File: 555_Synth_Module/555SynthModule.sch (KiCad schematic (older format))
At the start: 32 parts, among them J1 Conn_01x09_Male, Q1 2N3904, Q2 2N3904, Q3 2N3904, Q4 2N3904, Q5 2N3904, U1 NE555P, U2 LM741

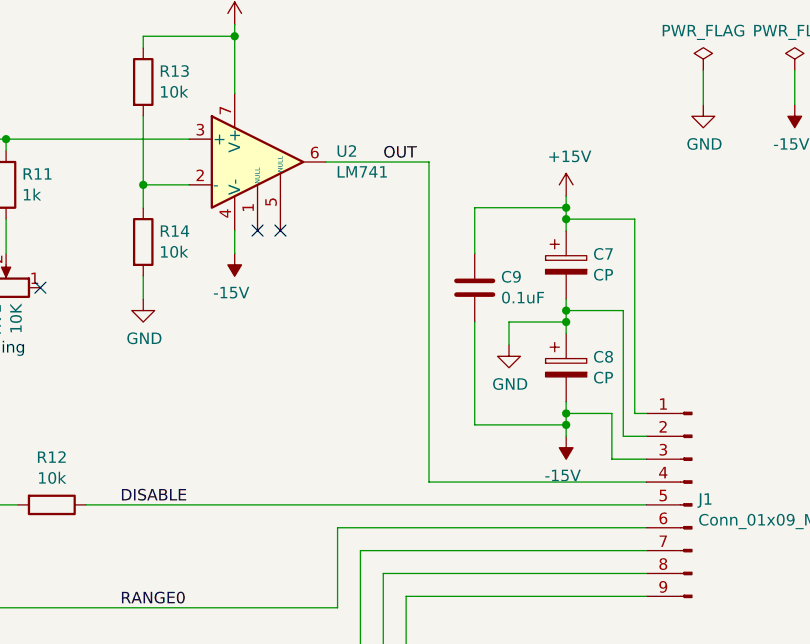
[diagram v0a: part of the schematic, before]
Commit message: Resolved Issue #3 Also: * Added output cap to 555 modules * EnvelopeFilter now has an output cap
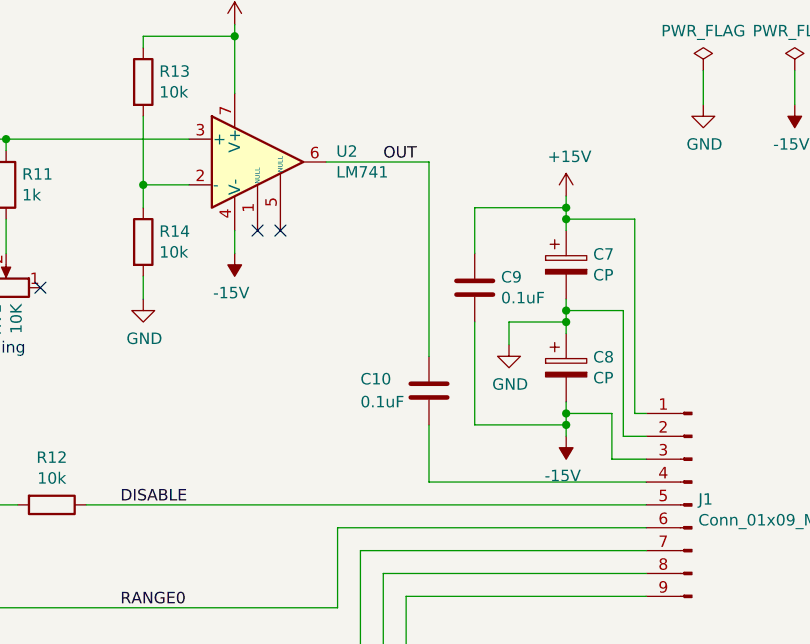
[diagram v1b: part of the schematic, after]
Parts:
- added C10: 0.1uF, Capacitor_THT:C_Disc_D4.3mm_W1.9mm_P5.00mm, symbol Device:C
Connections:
- net OUT: now also C10.1; no longer J1.4 (Pin_4)
- new net: C10.2, J1.4 (Pin_4)
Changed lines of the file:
@@
 	6950 2550 7400 2550
 Wire Wire Line
-	7400 2550 7400 3950
+	7400 2550 7400 3400
 $Comp
 L power:-15V #PWR0107
@@
 Wire Wire Line
 	5900 4050 8350 4050
+$Comp
+L Device:C C10
+U 1 1 602BE631
+P 7400 3550
+F 0 "C10" H 7100 3600 50  0000 L CNN
+F 1 "0.1uF" H 7100 3500 50  0000 L CNN
+F 2 "Capacitor_THT:C_Disc_D4.3mm_W1.9mm_P5.00mm" H 7438 3400 50  0001 C CNN
+F 3 "~" H 7400 3550 50  0001 C CNN
+	1    7400 3550
+	1    0    0    -1
+$EndComp
+Wire Wire Line
+	7400 3700 7400 3950
 $EndSCHEMATC
